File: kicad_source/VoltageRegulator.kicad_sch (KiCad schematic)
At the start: 39 parts, among them J10 x, J11 PowerPole, J12 Conn_01x02, Q2 IPD90P03P4L- 04, U12 INA226, U13 IFX91041EFJ

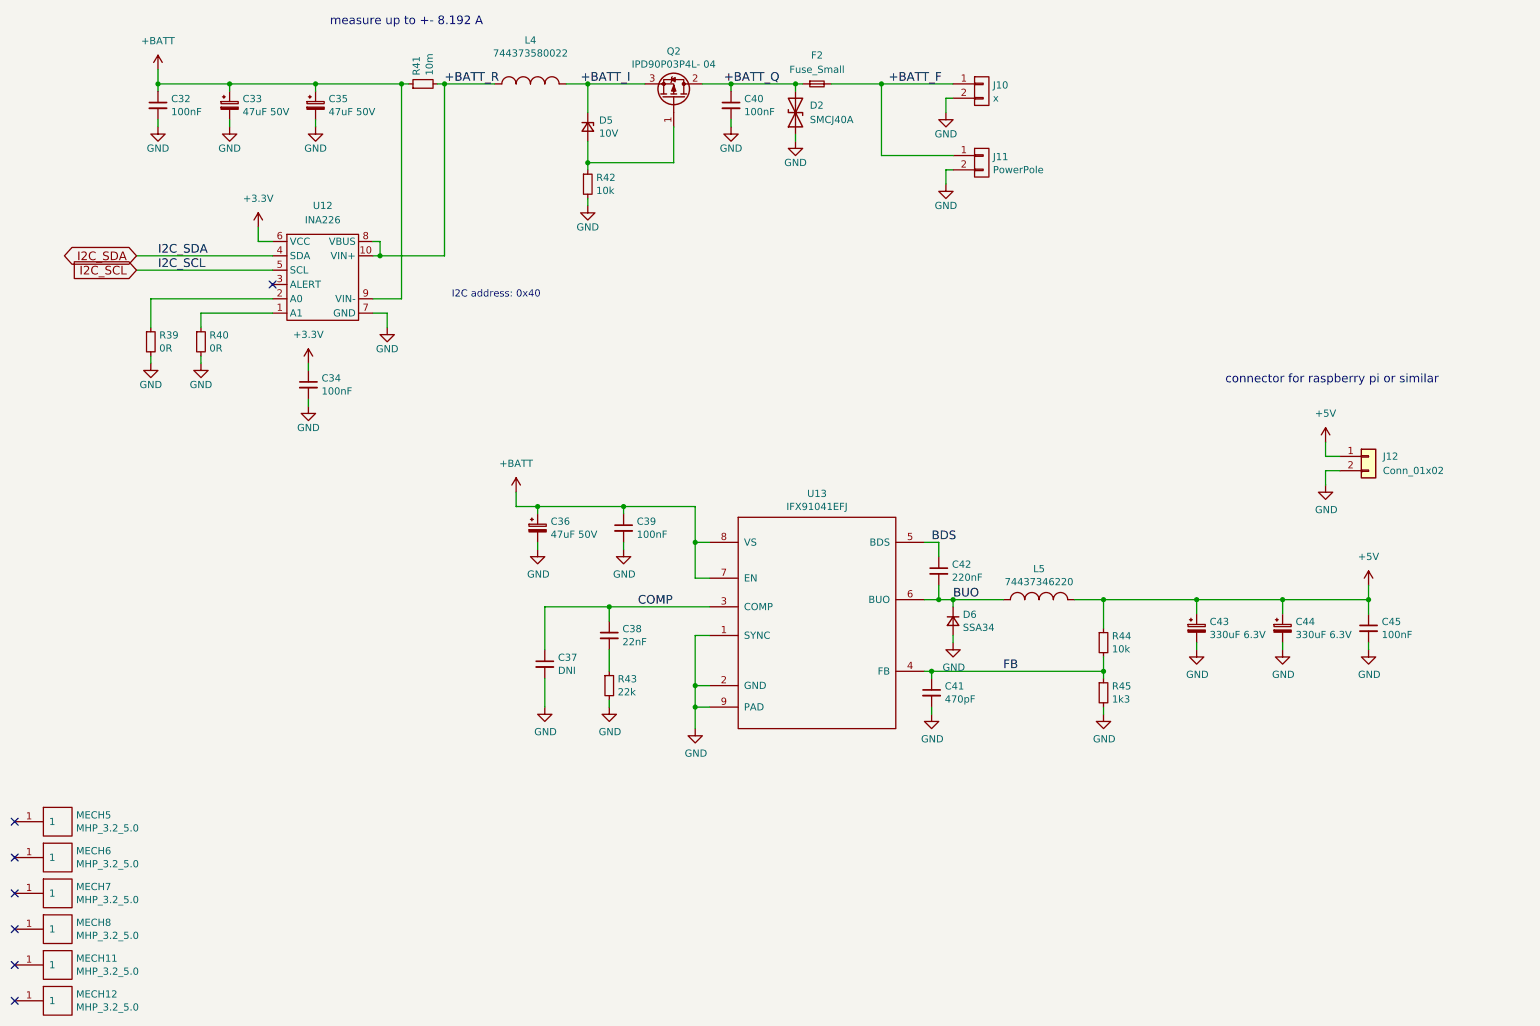
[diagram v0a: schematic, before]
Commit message: replaced tantal with electrolytic capacitors
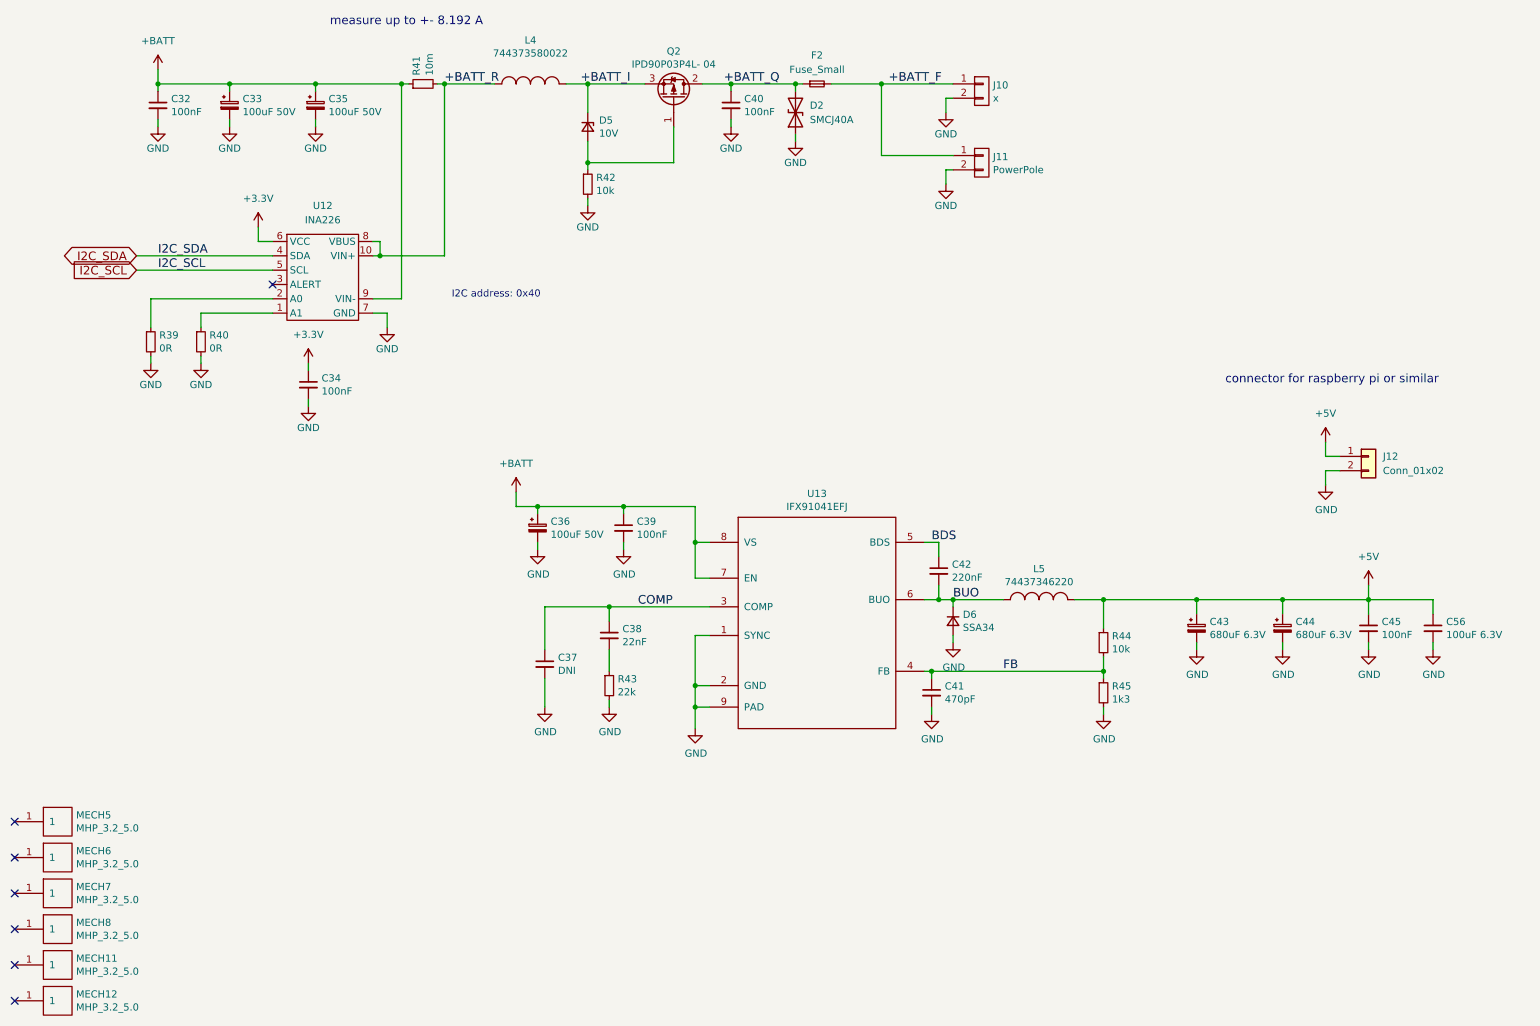
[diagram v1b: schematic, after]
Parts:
- added C56: 100uF 6.3V, Capacitor_SMD:C_1210_3225Metric, symbol Device:C_Small
- C33, C35, C36: value 47uF 50V -> 100uF 50V; footprint Capacitor_Tantalum_SMD:CP_EIA-7343-15_Kemet-W -> Capacitor_SMD:CP_Elec_6.3x7.7
- C43, C44: value 330uF 6.3V -> 680uF 6.3V; footprint Capacitor_Tantalum_SMD:CP_EIA-7343-15_Kemet-W -> Capacitor_SMD:CP_Elec_6.3x7.7
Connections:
- net +5V: now also C56.1
- net GND: now also C56.2
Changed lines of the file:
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@@
+    (stroke (width 0) (type default) (color 0 0 0 0))
+  )
+  (wire (pts (xy 274.32 128.27) (xy 274.32 129.54))
     (stroke (width 0) (type default) (color 0 0 0 0))
   )
@@
   )
   (wire (pts (xy 184.15 133.35) (xy 185.42 133.35))
+    (stroke (width 0) (type default) (color 0 0 0 0))
+  )
+  (wire (pts (xy 274.32 120.65) (xy 274.32 123.19))
+    (stroke (width 0) (type default) (color 0 0 0 0))
+  )
+  (wire (pts (xy 262.89 120.65) (xy 274.32 120.65))
     (stroke (width 0) (type default) (color 0 0 0 0))
   )
@@
       (effects (font (size 1.27 1.27)) (justify left))
     )
-    (property "Value" "330uF 6.3V" (id 1) (at 234.7214 126.873 0)
-      (effects (font (size 1.27 1.27)) (justify left))
-    )
-    (property "Footprint" "Capacitor_Tantalum_SMD:CP_EIA-7343-15_Kemet-W" (id 2) (at 234.95 130.81 0)
+    (property "Value" "680uF 6.3V" (id 1) (at 234.7214 126.873 0)
+      (effects (font (size 1.27 1.27)) (justify left))
+    )
+    (property "Footprint" "Capacitor_SMD:CP_Elec_6.3x7.7" (id 2) (at 234.95 130.81 0)
       (effects (font (size 1.27 1.27)) hide)
     )
@@
       (effects (font (size 1.27 1.27)) (justify left))
     )
-    (property "Value" "330uF 6.3V" (id 1) (at 249.9614 126.873 0)
-      (effects (font (size 1.27 1.27)) (justify left))
-    )
-    (property "Footprint" "Capacitor_Tantalum_SMD:CP_EIA-7343-15_Kemet-W" (id 2) (at 250.19 130.81 0)
+    (property "Value" "680uF 6.3V" (id 1) (at 249.9614 126.873 0)
+      (effects (font (size 1.27 1.27)) (justify left))
+    )
+    (property "Footprint" "Capacitor_SMD:CP_Elec_6.3x7.7" (id 2) (at 250.19 130.81 0)
       (effects (font (size 1.27 1.27)) hide)
     )
@@
       (effects (font (size 1.27 1.27)) (justify left))
     )
-    (property "Value" "47uF 50V" (id 1) (at 117.8814 109.093 0)
-      (effects (font (size 1.27 1.27)) (justify left))
-    )
-    (property "Footprint" "Capacitor_Tantalum_SMD:CP_EIA-7343-15_Kemet-W" (id 2) (at 118.11 113.03 0)
+    (property "Value" "100uF 50V" (id 1) (at 117.8814 109.093 0)
+      (effects (font (size 1.27 1.27)) (justify left))
+    )
+    (property "Footprint" "Capacitor_SMD:CP_Elec_6.3x7.7" (id 2) (at 118.11 113.03 0)
       (effects (font (size 1.27 1.27)) hide)
     )
@@
       (effects (font (size 1.27 1.27)) (justify left))
     )
-    (property "Value" "47uF 50V" (id 1) (at 63.2714 34.163 0)
-      (effects (font (size 1.27 1.27)) (justify left))
-    )
-    (property "Footprint" "Capacitor_Tantalum_SMD:CP_EIA-7343-15_Kemet-W" (id 2) (at 63.5 38.1 0)
+    (property "Value" "100uF 50V" (id 1) (at 63.2714 34.163 0)
+      (effects (font (size 1.27 1.27)) (justify left))
+    )
+    (property "Footprint" "Capacitor_SMD:CP_Elec_6.3x7.7" (id 2) (at 63.5 38.1 0)
       (effects (font (size 1.27 1.27)) hide)
     )
@@
       (effects (font (size 1.27 1.27)) (justify left))
     )
-    (property "Value" "47uF 50V" (id 1) (at 78.5114 34.163 0)
-      (effects (font (size 1.27 1.27)) (justify left))
-    )
-    (property "Footprint" "Capacitor_Tantalum_SMD:CP_EIA-7343-15_Kemet-W" (id 2) (at 78.74 38.1 0)
+    (property "Value" "100uF 50V" (id 1) (at 78.5114 34.163 0)
+      (effects (font (size 1.27 1.27)) (justify left))
+    )
+    (property "Footprint" "Capacitor_SMD:CP_Elec_6.3x7.7" (id 2) (at 78.74 38.1 0)
       (effects (font (size 1.27 1.27)) hide)
     )
@@
     (pin "1")
   )
+  (symbol (lib_id "Device:C_Small") (at 274.32 125.73 0) (unit 1)
+    (in_bom yes) (on_board yes)
+    (property "Reference" "C56" (id 0) (at 276.6568 124.5616 0)
+      (effects (font (size 1.27 1.27)) (justify left))
+    )
+    (property "Value" "100uF 6.3V" (id 1) (at 276.6568 126.873 0)
+      (effects (font (size 1.27 1.27)) (justify left))
+    )
+    (property "Footprint" "Capacitor_SMD:C_1210_3225Metric" (id 2) (at 274.32 129.54 0)
+      (effects (font (size 1.27 1.27)) hide)
+    )
+    (property "Datasheet" "" (id 3) (at 274.32 125.73 0))
+    (pin "1")
+    (pin "2")
+  )
   (symbol (lib_id "Device:R_Small") (at 46.99 74.93 0) (unit 1)
     (in_bom yes) (on_board yes)
@@
     (pin "2")
   )
+  (symbol (lib_id "power:GND") (at 274.32 129.54 0) (unit 1)
+    (in_bom yes) (on_board yes)
+    (property "Reference" "#PWR044" (id 0) (at 274.32 135.89 0)
+      (effects (font (size 1.27 1.27)) hide)
+    )
+    (property "Value" "GND" (id 1) (at 274.447 133.9342 0))
+    (property "Footprint" "" (id 2) (at 274.32 129.54 0))
+    (property "Datasheet" "" (id 3) (at 274.32 129.54 0))
+    (pin "1")
+  )
 )

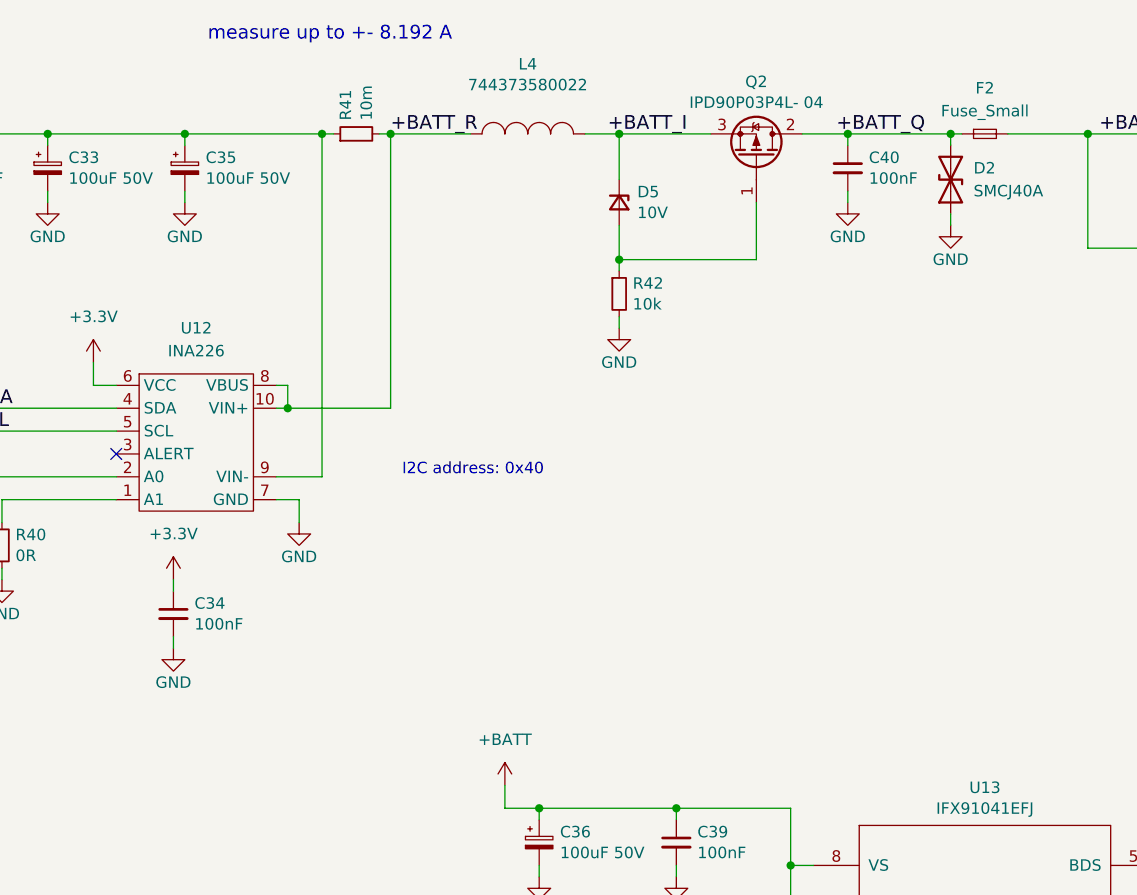
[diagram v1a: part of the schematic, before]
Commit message: checked supply voltage of parts
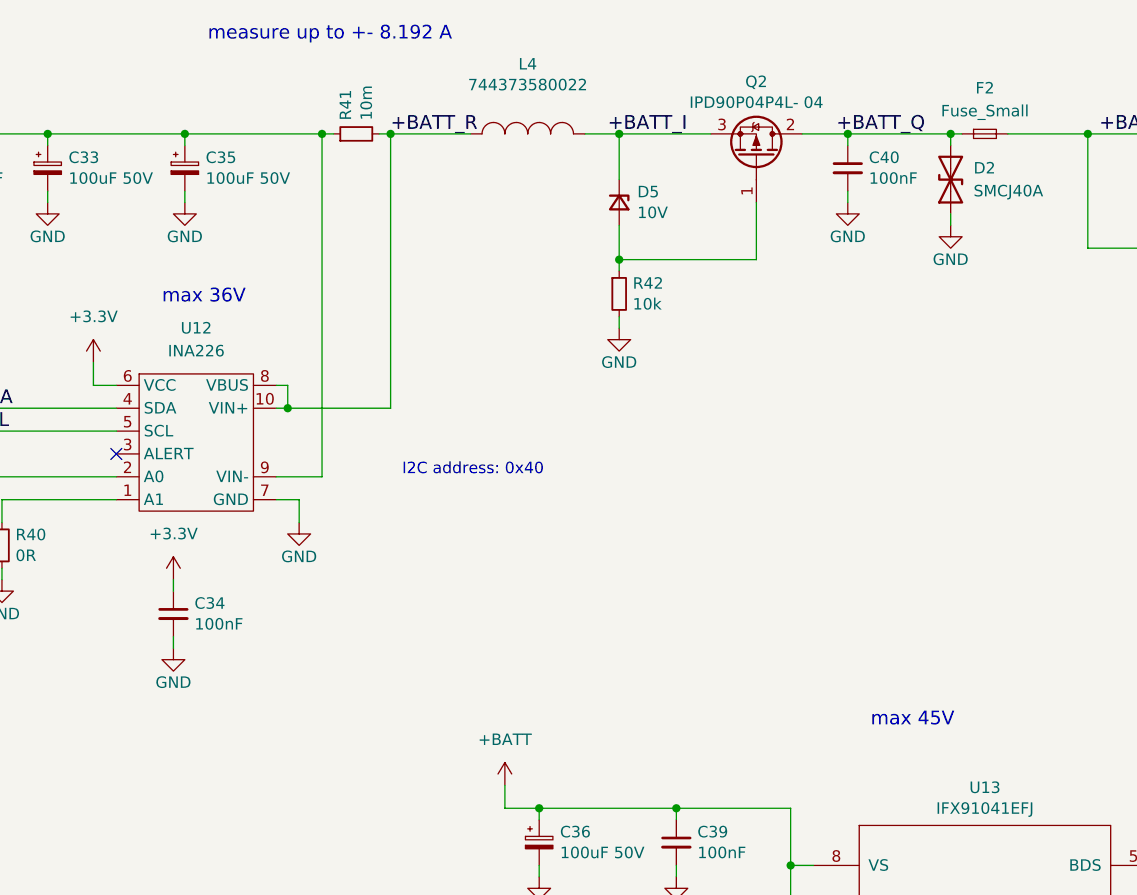
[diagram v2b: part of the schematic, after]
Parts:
- L4: footprint Inductor_SMD:L_Wuerth_HCI-7050 -> Inductor_SMD:L_Wuerth_HCM-1052
- Q2: value IPD90P03P4L- 04 -> IPD90P04P4L- 04
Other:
- note added: "max 36V"
- note added: "max 45V"
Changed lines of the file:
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@@
+    (effects (font (size 1.524 1.524)) (justify left bottom))
+  )
+  (text "max 36V" (at 73.66 48.26 0)
+    (effects (font (size 1.524 1.524)) (justify left bottom))
+  )
+  (text "max 45V" (at 152.4 95.25 0)
     (effects (font (size 1.524 1.524)) (justify left bottom))
   )
@@
     (property "Reference" "L4" (id 0) (at 114.3 21.463 0))
     (property "Value" "744373580022" (id 1) (at 114.3 23.7744 0))
-    (property "Footprint" "Inductor_SMD:L_Wuerth_HCI-7050" (id 2) (at 114.3 26.0858 0)
+    (property "Footprint" "Inductor_SMD:L_Wuerth_HCM-1052" (id 2) (at 114.3 26.0858 0)
       (effects (font (size 1.27 1.27)) hide)
     )
@@
     (in_bom yes) (on_board yes)
     (property "Reference" "Q2" (id 0) (at 139.7 23.4188 90))
-    (property "Value" "IPD90P03P4L- 04" (id 1) (at 139.7 25.7302 90))
+    (property "Value" "IPD90P04P4L- 04" (id 1) (at 139.7 25.7302 90))
     (property "Footprint" "Package_TO_SOT_SMD:TO-252-2" (id 2) (at 142.24 26.67 0)
       (effects (font (size 1.27 1.27)) hide)
